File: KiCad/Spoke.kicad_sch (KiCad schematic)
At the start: 134 parts, among them J1 B2B-PH-K-S, J10 BL-A, J11 BL-C, J12 Amphenol 132289, J2 BAT+, J3 BAT-, J4 GCT USB4105/USB4110, J5 USB+, J6 USB-, J7 PLS-1x3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

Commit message: Export SCH and BOM
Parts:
- J10, J11, J2, J3, J5, J6, TP1, TP10, TP11, TP12, TP13, TP14, TP15, TP16, TP17, TP18, TP2, TP3, TP4, TP5, TP6, TP7, TP8, TP9: now left out of the parts list
- SW1: value PWR -> ~
- SW2: value OK/UP -> ~
- SW3: value ESC/DN -> ~
- SW4: value BOOT -> ~
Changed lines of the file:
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@@
 		(unit 1)
 		(exclude_from_sim no)
-		(in_bom yes)
+		(in_bom no)
 		(on_board yes)
 		(dnp no)
@@
 		)
 		(property "Description" ""
-			(at 346.71 203.2 0)
+			(at 341.63 207.01 0)
 			(effects
 				(font
@@
 		(unit 1)
 		(exclude_from_sim no)
-		(in_bom yes)
+		(in_bom no)
 		(on_board yes)
 		(dnp no)
@@
 		(unit 1)
 		(exclude_from_sim no)
-		(in_bom yes)
+		(in_bom no)
 		(on_board yes)
 		(dnp no)
@@
 		(unit 1)
 		(exclude_from_sim no)
-		(in_bom yes)
+		(in_bom no)
 		(on_board yes)
 		(dnp no)
@@
 		(unit 1)
 		(exclude_from_sim no)
-		(in_bom yes)
+		(in_bom no)
 		(on_board yes)
 		(dnp no)
@@
 		(unit 1)
 		(exclude_from_sim no)
-		(in_bom yes)
+		(in_bom no)
 		(on_board yes)
 		(dnp no)
@@
 		)
 		(property "Value" "~"
-			(at 236.22 58.42 0)
+			(at 236.22 67.31 0)
 			(effects
 				(font
@@
 		(unit 1)
 		(exclude_from_sim no)
-		(in_bom yes)
+		(in_bom no)
 		(on_board yes)
 		(dnp no)
@@
 		(unit 1)
 		(exclude_from_sim no)
-		(in_bom yes)
+		(in_bom no)
 		(on_board yes)
 		(dnp no)
@@
 		)
 		(property "Description" ""
-			(at 134.62 349.25 0)
+			(at 139.7 353.06 0)
 			(effects
 				(font
@@
 		(unit 1)
 		(exclude_from_sim no)
-		(in_bom yes)
+		(in_bom no)
 		(on_board yes)
 		(dnp no)
@@
 		(unit 1)
 		(exclude_from_sim no)
-		(in_bom yes)
+		(in_bom no)
 		(on_board yes)
 		(dnp no)
@@
 		(unit 1)
 		(exclude_from_sim no)
-		(in_bom yes)
+		(in_bom no)
 		(on_board yes)
 		(dnp no)
@@
 		(unit 1)
 		(exclude_from_sim no)
-		(in_bom yes)
+		(in_bom no)
 		(on_board yes)
 		(dnp no)
@@
 		(unit 1)
 		(exclude_from_sim no)
-		(in_bom yes)
+		(in_bom no)
 		(on_board yes)
 		(dnp no)
@@
 			)
 		)
-		(property "Value" "OK/UP"
+		(property "Value" "~"
 			(at 72.39 143.51 0)
 			(effects
@@
 					(size 1.27 1.27)
 				)
+				(hide yes)
 			)
 		)
@@
 			)
 		)
-		(property "Description" ""
-			(at 81.28 130.81 0)
+		(property "Description" "OK/UP"
+			(at 72.39 143.51 0)
 			(effects
 				(font
 					(size 1.27 1.27)
 				)
-				(hide yes)
 			)
 		)
@@
 		(unit 1)
 		(exclude_from_sim no)
-		(in_bom yes)
+		(in_bom no)
 		(on_board yes)
 		(dnp no)
@@
 			)
 		)
-		(property "Value" "ESC/DN"
+		(property "Value" "~"
 			(at 72.39 168.91 0)
 			(effects
@@
 					(size 1.27 1.27)
 				)
+				(hide yes)
 			)
 		)
@@
 			)
 		)
-		(property "Description" ""
-			(at 81.28 156.21 0)
+		(property "Description" "ESC/DN"
+			(at 72.39 168.91 0)
 			(effects
 				(font
 					(size 1.27 1.27)
 				)
-				(hide yes)
 			)
 		)
@@
 		(unit 1)
 		(exclude_from_sim no)
-		(in_bom yes)
+		(in_bom no)
 		(on_board yes)
 		(dnp no)
@@
 		(unit 1)
 		(exclude_from_sim no)
-		(in_bom yes)
+		(in_bom no)
 		(on_board yes)
 		(dnp no)
@@
 		(dnp no)
 		(property "Reference" "SW4"
-			(at 207.01 209.55 0)
+			(at 207.01 210.82 0)
 			(effects
 				(font
@@
 			)
 		)
-		(property "Value" "BOOT"
+		(property "Value" "~"
 			(at 207.01 224.79 0)
 			(effects
@@
 					(size 1.27 1.27)
 				)
+				(hide yes)
 			)
 		)
@@
 			)
 		)
-		(property "Description" ""
-			(at 215.9 212.09 0)
+		(property "Description" "BOOT"
+			(at 207.01 223.52 0)
 			(effects
 				(font
 					(size 1.27 1.27)
 				)
-				(hide yes)
 			)
 		)
@@
 		)
 		(property "Description" ""
-			(at 346.71 215.9 0)
+			(at 341.63 219.71 0)
 			(effects
 				(font
@@
 		(unit 1)
 		(exclude_from_sim no)
-		(in_bom yes)
+		(in_bom no)
 		(on_board yes)
 		(dnp no)
@@
 		(unit 1)
 		(exclude_from_sim no)
-		(in_bom yes)
+		(in_bom no)
 		(on_board yes)
 		(dnp no)
@@
 		(unit 1)
 		(exclude_from_sim no)
-		(in_bom yes)
+		(in_bom no)
 		(on_board yes)
 		(dnp no)
@@
 		(unit 1)
 		(exclude_from_sim no)
-		(in_bom yes)
+		(in_bom no)
 		(on_board yes)
 		(dnp no)
@@
 			)
 		)
-		(property "Value" "PWR"
+		(property "Value" "~"
 			(at 72.39 93.98 0)
 			(effects
@@
 					(size 1.27 1.27)
 				)
+				(hide yes)
 			)
 		)
@@
 			)
 		)
-		(property "Description" ""
-			(at 81.28 81.28 0)
+		(property "Description" "PWR"
+			(at 72.39 93.98 0)
 			(effects
 				(font
 					(size 1.27 1.27)
 				)
-				(hide yes)
 			)
 		)
@@
 		(unit 1)
 		(exclude_from_sim no)
-		(in_bom yes)
+		(in_bom no)
 		(on_board yes)
 		(dnp no)
@@
 		(unit 1)
 		(exclude_from_sim no)
-		(in_bom yes)
+		(in_bom no)
 		(on_board yes)
 		(dnp no)
@@
 		(unit 1)
 		(exclude_from_sim no)
-		(in_bom yes)
+		(in_bom no)
 		(on_board yes)
 		(dnp no)
@@
 		(unit 1)
 		(exclude_from_sim no)
-		(in_bom yes)
+		(in_bom no)
 		(on_board yes)
 		(dnp no)

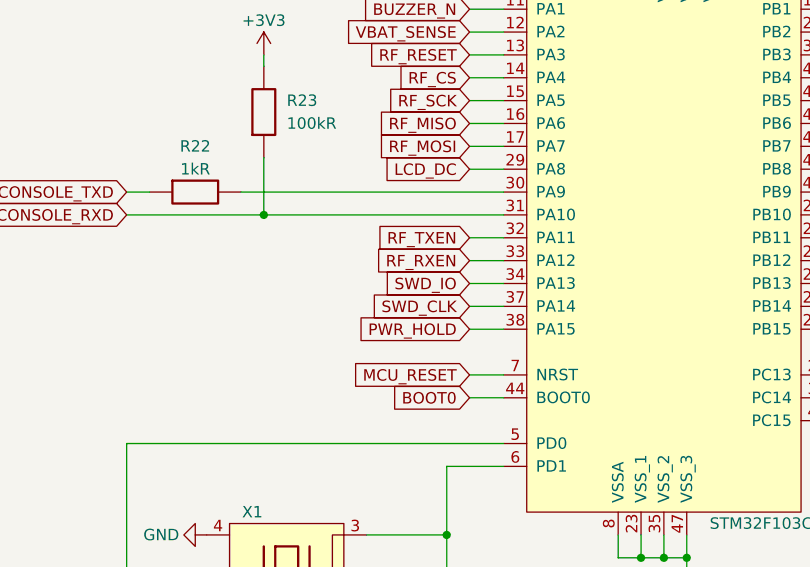
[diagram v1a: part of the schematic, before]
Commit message: Swap PWR_HOLD and RF_TXEN; re-route
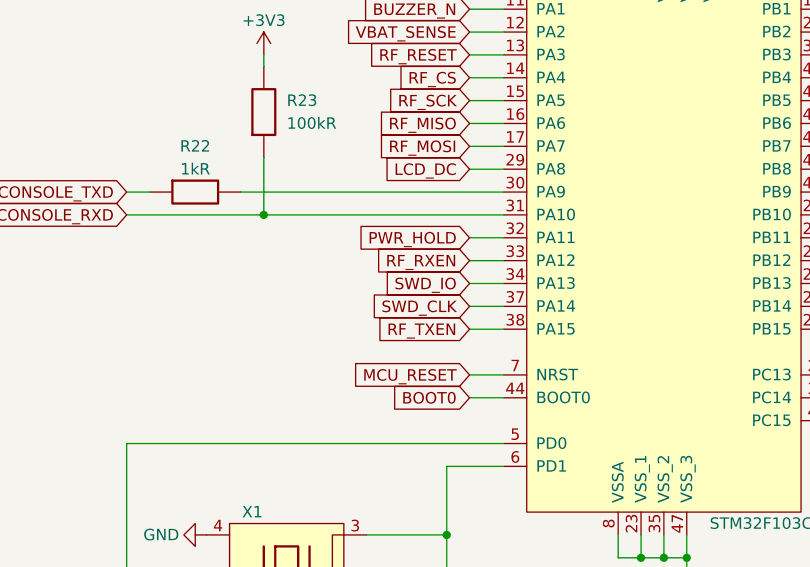
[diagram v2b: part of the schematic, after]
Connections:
- net PWR_HOLD: now also U6.32 (PA11); no longer U6.38 (PA15)
- net RF_TXEN: now also U6.38 (PA15); no longer U6.32 (PA11)

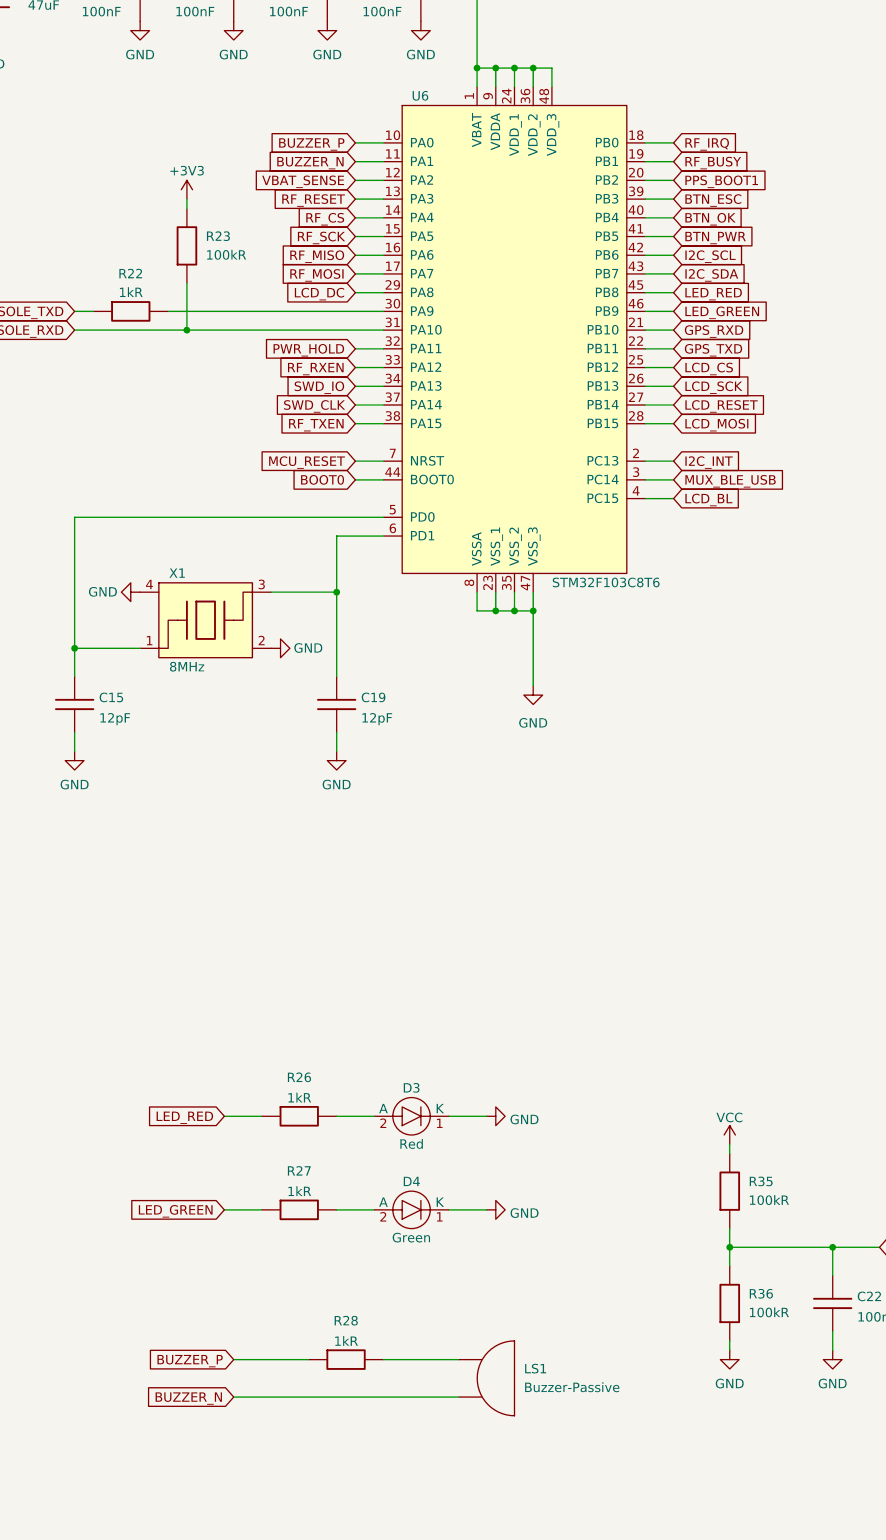
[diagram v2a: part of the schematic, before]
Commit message: Move LCD_BL to PA1 (ex BUZZER_N)
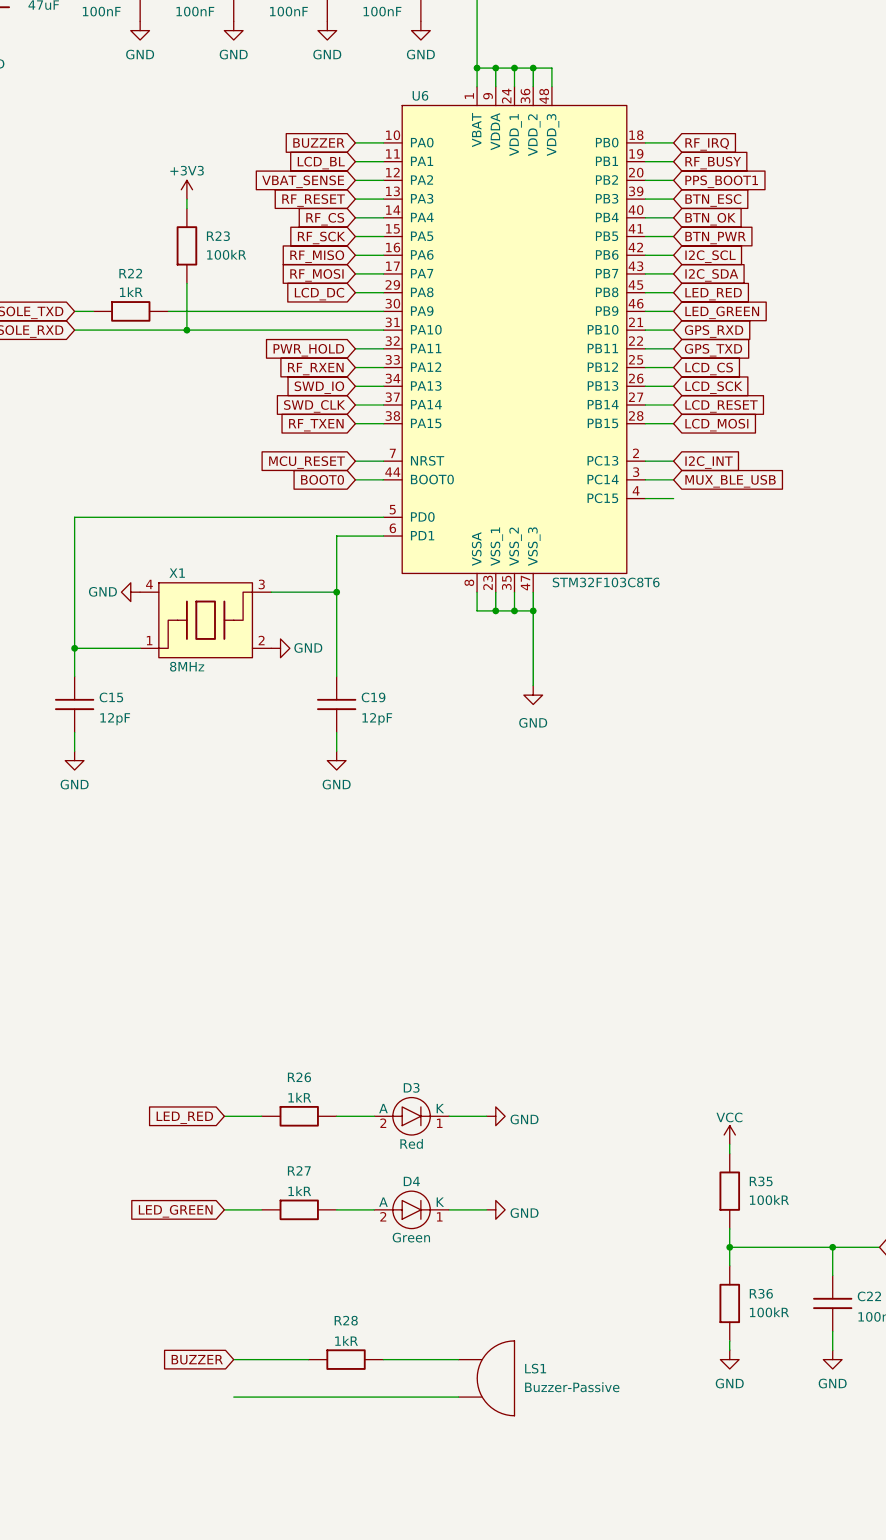
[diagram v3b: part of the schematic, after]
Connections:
- net LCD_BL: now also U6.11 (PA1); no longer U6.4 (PC15)
- net BUZZER_N: no longer names the net of LS1.2
- net BUZZER_N: no longer U6.11 (PA1)
- net BUZZER_P renamed BUZZER
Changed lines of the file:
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@@
-		)
-	)
-	(global_label "BUZZER_N"
-		(shape input)
-		(at 317.5 241.3 180)
-		(fields_autoplaced yes)
-		(effects
-			(font
-				(size 1.27 1.27)
-			)
-			(justify right)
-		)
-		(property "Intersheetrefs" "${INTERSHEET_REFS}"
-			(at 305.3502 241.2206 0)
-			(effects
-				(font
-					(size 1.27 1.27)
-				)
-				(justify right)
-				(hide yes)
-			)
 		)
 	)
@@
 		)
 	)
-	(global_label "BUZZER_P"
+	(global_label "BUZZER"
 		(shape input)
 		(at 334.01 71.12 180)
@@
 		)
 		(property "Intersheetrefs" "${INTERSHEET_REFS}"
-			(at 321.9207 71.0406 0)
+			(at 323.5863 71.12 0)
 			(effects
 				(font
@@
 		)
 	)
-	(global_label "BUZZER_P"
+	(global_label "BUZZER"
 		(shape input)
 		(at 317.5 236.22 180)
@@
 		)
 		(property "Intersheetrefs" "${INTERSHEET_REFS}"
-			(at 305.4107 236.1406 0)
+			(at 307.0763 236.22 0)
 			(effects
 				(font
@@
 	(global_label "LCD_BL"
 		(shape input)
-		(at 377.19 119.38 0)
-		(fields_autoplaced yes)
-		(effects
-			(font
-				(size 1.27 1.27)
-			)
-			(justify left)
-		)
-		(property "Intersheetrefs" "${INTERSHEET_REFS}"
-			(at 387.009 119.38 0)
-			(effects
-				(font
-					(size 1.27 1.27)
-				)
-				(justify left)
-				(hide yes)
-			)
-		)
-	)
-	(global_label "BUZZER_N"
-		(shape input)
 		(at 334.01 73.66 180)
 		(fields_autoplaced yes)
@@
 		)
 		(property "Intersheetrefs" "${INTERSHEET_REFS}"
-			(at 321.8602 73.5806 0)
-			(effects
-				(font
+			(at 324.191 73.66 0)
+			(effects
+				(font

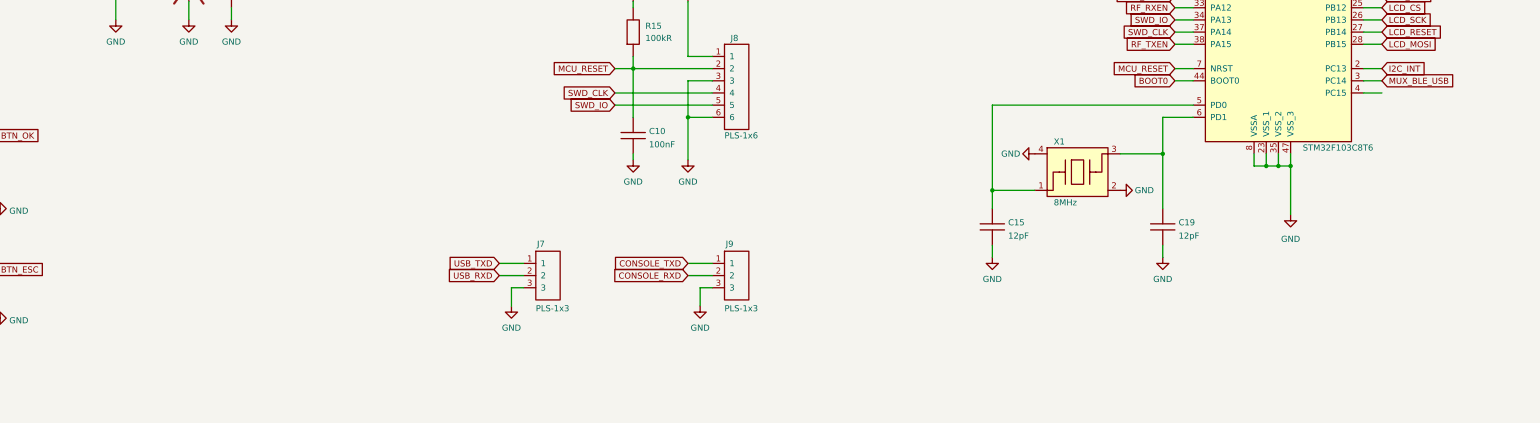
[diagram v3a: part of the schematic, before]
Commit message: Add ALARM button
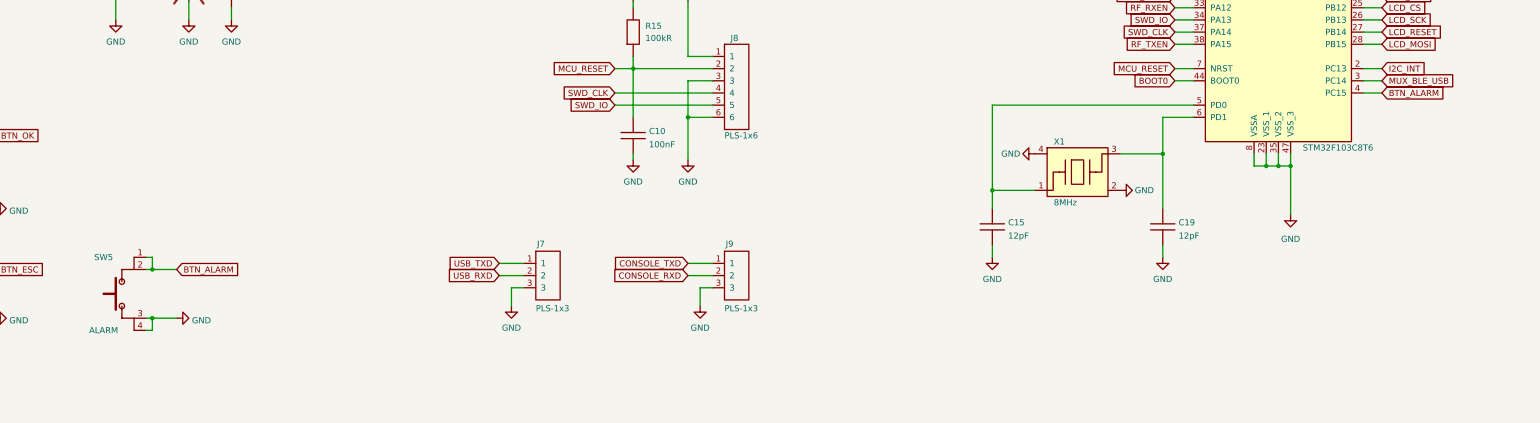
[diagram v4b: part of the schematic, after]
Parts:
- added SW5: ~, Spoke:Button_6x6, symbol Spoke:Button-SPST-NO
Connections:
- net GND: now also SW5.3 (2), SW5.4 (2)
- net BTN_ALARM: now reaches U6.4 (PC15)
- net BTN_ALARM: now also SW5.1, SW5.2

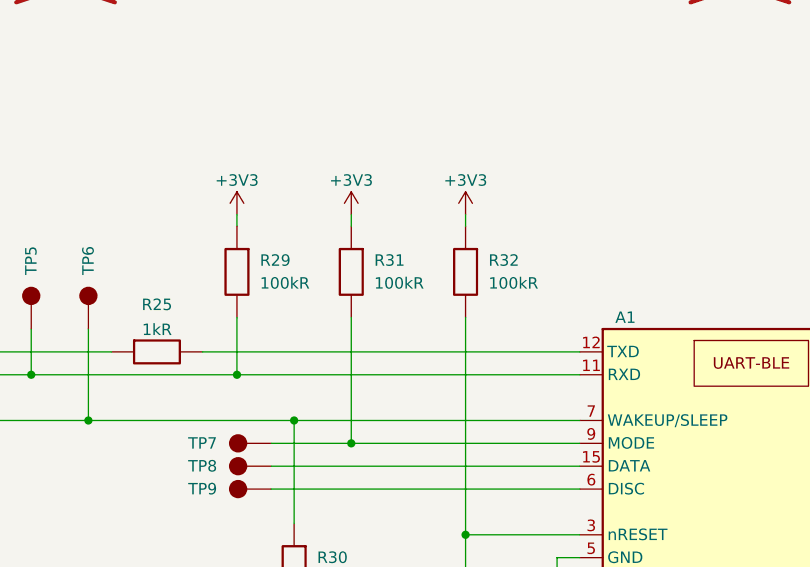
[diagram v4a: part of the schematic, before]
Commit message: Replace R31 to 1 kOhm
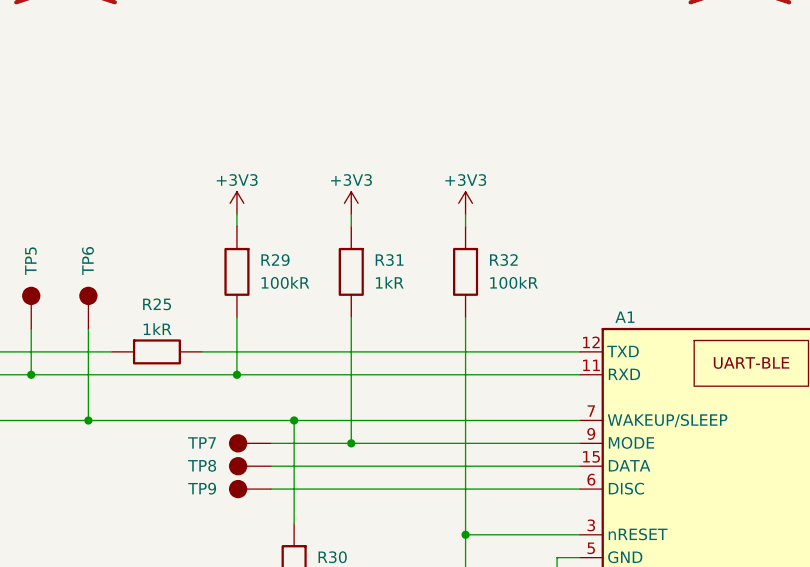
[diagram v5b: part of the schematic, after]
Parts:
- R31: value 100kR -> 1kR
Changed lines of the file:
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@@
 			)
 		)
-		(property "Value" "100kR"
+		(property "Value" "1kR"
 			(at 342.9 327.6599 90)
 			(effects
